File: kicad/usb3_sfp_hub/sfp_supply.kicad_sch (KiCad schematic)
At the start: 9 parts, among them J8 Supply test access / footprin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, U7 TPS62902RPJR

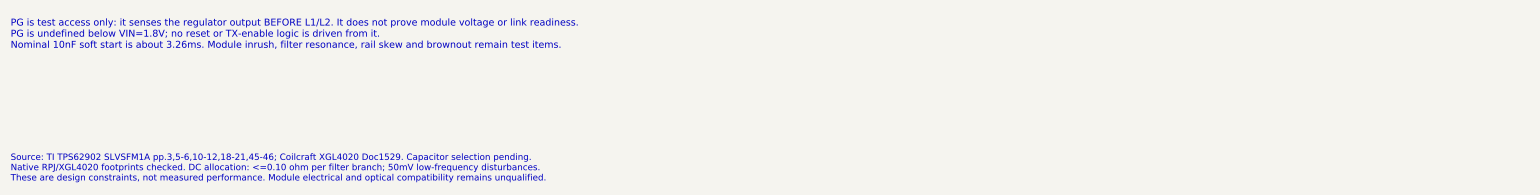
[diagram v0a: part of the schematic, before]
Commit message: usb3_sfp_hub: source JLCPCB parts; 3x3mm filter inductors and damping resistor
L1/L2: replace the unavailable Coilcraft XGL4020-472MEC (LCSC stock 1) with cjiang FTC303018D4R7MBCA (LCSC C5832388), 3x3mm matching the calipered reference board, on Inductor_SMD:L_Changjiang_FTC303020D.

R1/R2: replace the untraceable Panasonic ERJ8RQFR43V (no LCSC listing) with FH RTF06KR430FTG (LCSC C44453441), same 0.43 ohm 1% 1206 current-sense damping.

- Assign LCSC/JLCPCB numbers to the settled passives and ICs; export to bom.csv.
- Rebase check_sfp_power_budget on the real 72mOhm filter DCR and report the 0.10 ohm allocation gap instead of asserting it away.
- Regenerate the six sheets, netlist, budget JSON, BOM and previews; update README and sfp_filter_evidence.json.
- Drop stale analyzer dumps (bom/analysis.json, validation/schematic_analysis.json) and ignore the regenerated copies.

Connectivity check PASS (105 components). ERC and full analog/optical qualification remain open; no PCB.
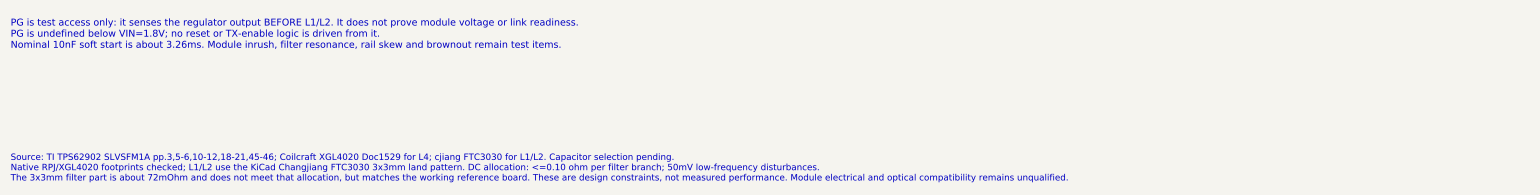
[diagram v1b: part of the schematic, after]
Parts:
- C55: LCSC (none) -> C1525; MPN (none) -> CL05B104KO5NNNC; Manufacturer (none) -> Samsung Electro-Mechanics
- L4: LCSC (none) -> C5357696
- R22: LCSC (none) -> C2998122; MPN (none) -> FRC0603F3242TS; Manufacturer (none) -> FOJAN
- R23: LCSC (none) -> C25804; MPN (none) -> 0603WAF1002T5E; Manufacturer (none) -> UNI-ROYAL
- U7: LCSC (none) -> C2870154
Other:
- note added: "Source: TI TPS62902 SLVSFM1A pp.3,5-6,10-12,18-21,45-46; Coilcraft XGL4020 Doc1529 for L4; cjiang FTC3030 for L1/L2. Capacitor selection pending. Native RPJ/XGL4020 footprints checked; L1/L2 use the KiCad Changjiang FTC3030 3x3mm land pattern. DC allocation: <=0.10 ohm per filter branch; 50mV low-frequency disturbances. The 3x3mm filter part is about 72mOhm and does not meet that allocation, but 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"
- note removed: "Source: TI TPS62902 SLVSFM1A pp.3,5-6,10-12,18-21,45-46; Coilcraft XGL4020 Doc1529. Capacitor selection pending. Native RPJ/XGL4020 footprints checked. DC allocation: <=0.10 ohm per filter branch; 50mV low-frequency disturbances. These are design constraints, not measured performance. Module electrical and optical compatibility remains unqualified."
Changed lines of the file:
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@@
 (property "Datasheet" "https://www.ti.com/lit/ds/symlink/tps62902.pdf" (at 93.98 58.42 0) (effects (font (size 1 1)) hide))
 (property "BOM Comments" "RPJ nine-pad VQFN, no separate EP. Native local footprint from TI land pattern. VSET open=3.3V with 32.4k MODE; stock not verified." (at 93.98 58.42 0) (effects (font (size 1 1)) hide))
+(property "LCSC" "C2870154" (at 93.98 58.42 0) (effects (font (size 1 1)) hide))
 (pin "1")
 (pin "2")
@@
 (property "Datasheet" "https://www.coilcraft.com/getmedia/76c9c081-4945-4c85-9129-9356e1ad6734/xgl4020.pdf" (at 241.3 43.18 0) (effects (font (size 1 1)) hide))
 (property "BOM Comments" "TI Table 8-4 listed part; 9mOhm max DCR; 3.8/6.3/8.8A Isat at 10/20/30% drop at 25C; stripe faces pad1 SW; thermal/AC/fault peaks pending" (at 241.3 43.18 0) (effects (font (size 1 1)) hide))
+(property "LCSC" "C5357696" (at 241.3 43.18 0) (effects (font (size 1 1)) hide))
 (pin "1")
 (pin "2")
@@
 (property "Footprint" "Capacitor_SMD:C_0402_1005Metric" (at 93.98 177.8 0) (effects (font (size 1 1)) hide))
 (property "Placement target" "U7.6 to U7.4; minimize input switching loop" (at 93.98 177.8 0) (effects (font (size 1 1)) hide))
+(property "LCSC" "C1525" (at 93.98 177.8 0) (effects (font (size 1 1)) hide))
+(property "MPN" "CL05B104KO5NNNC" (at 93.98 177.8 0) (effects (font (size 1 1)) hide))
+(property "Manufacturer" "Samsung Electro-Mechanics" (at 93.98 177.8 0) (effects (font (size 1 1)) hide))
 (pin "1")
 (pin "2")
@@
 (property "Footprint" "Resistor_SMD:R_0603_1608Metric" (at 241.3 111.76 0) (effects (font (size 1 1)) hide))
 (property "BOM Comments" "TI Table 7-1 option 10: VSET, 2.5MHz, forced PWM, discharge enabled; total tolerance within +/-4%, pin C <=30pF" (at 241.3 111.76 0) (effects (font (size 1 1)) hide))
+(property "LCSC" "C2998122" (at 241.3 111.76 0) (effects (font (size 1 1)) hide))
+(property "MPN" "FRC0603F3242TS" (at 241.3 111.76 0) (effects (font (size 1 1)) hide))
+(property "Manufacturer" "FOJAN" (at 241.3 111.76 0) (effects (font (size 1 1)) hide))
 (pin "1")
 (pin "2")
@@
 (property "Value" "10k / 1%" (at 241.3 147.32 0) (effects (font (size 1 1))))
 (property "Footprint" "Resistor_SMD:R_0603_1608Metric" (at 241.3 144.78 0) (effects (font (size 1 1)) hide))
+(property "LCSC" "C25804" (at 241.3 144.78 0) (effects (font (size 1 1)) hide))
+(property "MPN" "0603WAF1002T5E" (at 241.3 144.78 0) (effects (font (size 1 1)) hide))
+(property "Manufacturer" "UNI-ROYAL" (at 241.3 144.78 0) (effects (font (size 1 1)) hide))
 (pin "1")
 (pin "2")
@@
 (text "U7 is independent of the hub 3.3V LDO. Both SFP filters share its output.\nMODE 32.4k selects forced PWM / 2.5MHz / VSET / discharge. Pin 9 deliberately OPEN selects 3.3V.\nEN follows local 5V. This sheet does not implement commanded module power cycling." (at 15.24 205.74 0) (effects (font (size 1.3 1.3)) (justify left top)))
 (text "PG is test access only: it senses the regulator output BEFORE L1/L2. It does not prove module voltage or link readiness.\nPG is undefined below VIN=1.8V; no reset or TX-enable logic is driven from it.\nNominal 10nF soft start is about 3.26ms. Module inrush, filter resonance, rail skew and brownout remain test items." (at 15.24 231.14 0) (effects (font (size 1.3 1.3)) (justify left top)))
-(text "Source: TI TPS62902 SLVSFM1A pp.3,5-6,10-12,18-21,45-46; Coilcraft XGL4020 Doc1529. Capacitor selection pending.\nNative RPJ/XGL4020 footprints checked. DC allocation: <=0.10 ohm per filter branch; 50mV low-frequency disturbances.\nThese are design constraints, not measured performance. Module electrical and optical compatibility remains unqualified." (at 15.24 256.54 0) (effects (font (size 1.2 1.2)) (justify left top)))
+(text "Source: TI TPS62902 SLVSFM1A pp.3,5-6,10-12,18-21,45-46; Coilcraft XGL4020 Doc1529 for L4; cjiang FTC3030 for L1/L2. Capacitor selection pending.\nNative RPJ/XGL4020 footprints checked; L1/L2 use the KiCad Changjiang FTC3030 3x3mm land pattern. DC allocation: <=0.10 ohm per filter branch; 50mV low-frequency disturbances.\nThe 3x3mm filter part is about 72mOhm and does not meet that allocation, but matches the working reference board. These are design constraints, not measured performance. Module electrical and optical compatibility remains unqualified." (at 15.24 256.54 0) (effects (font (size 1.2 1.2)) (justify left top)))
 (embedded_fonts no))
